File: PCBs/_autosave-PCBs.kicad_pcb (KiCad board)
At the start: 4 copper layers, 44.5 x 15.5 mm, 8 parts, among them P1 Input 1x2, P2 Output 1x2, U1 TPS62172DSGR

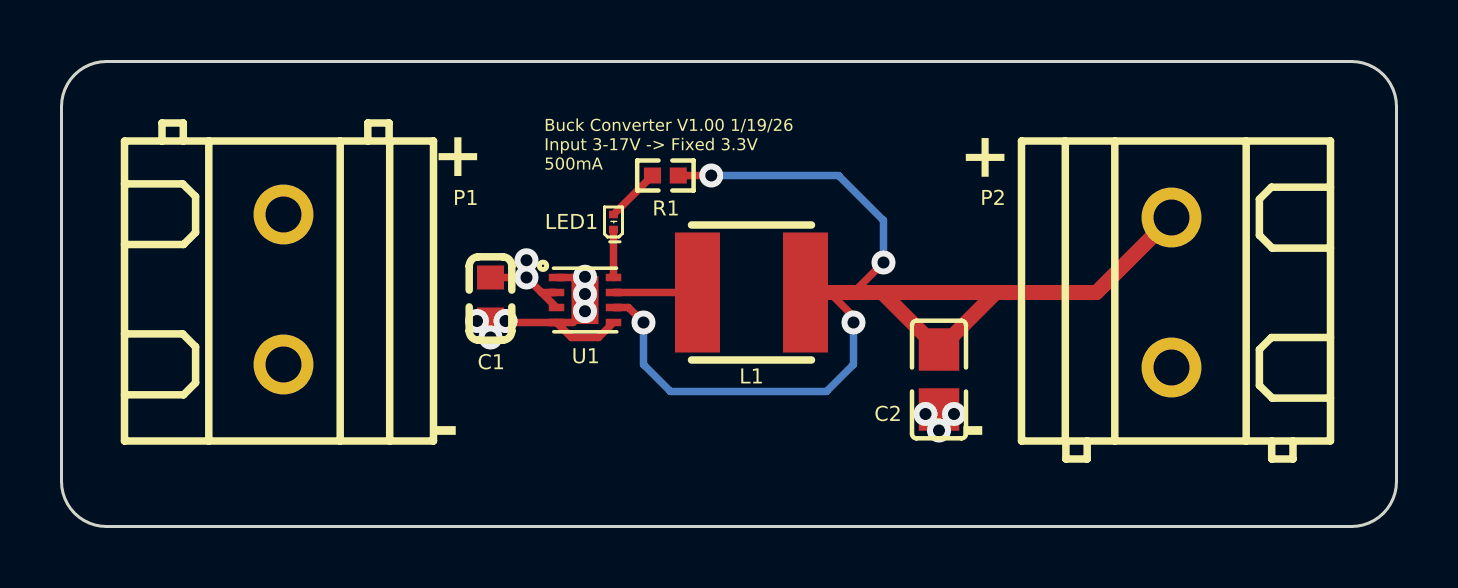
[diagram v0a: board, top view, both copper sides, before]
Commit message: buck converter done
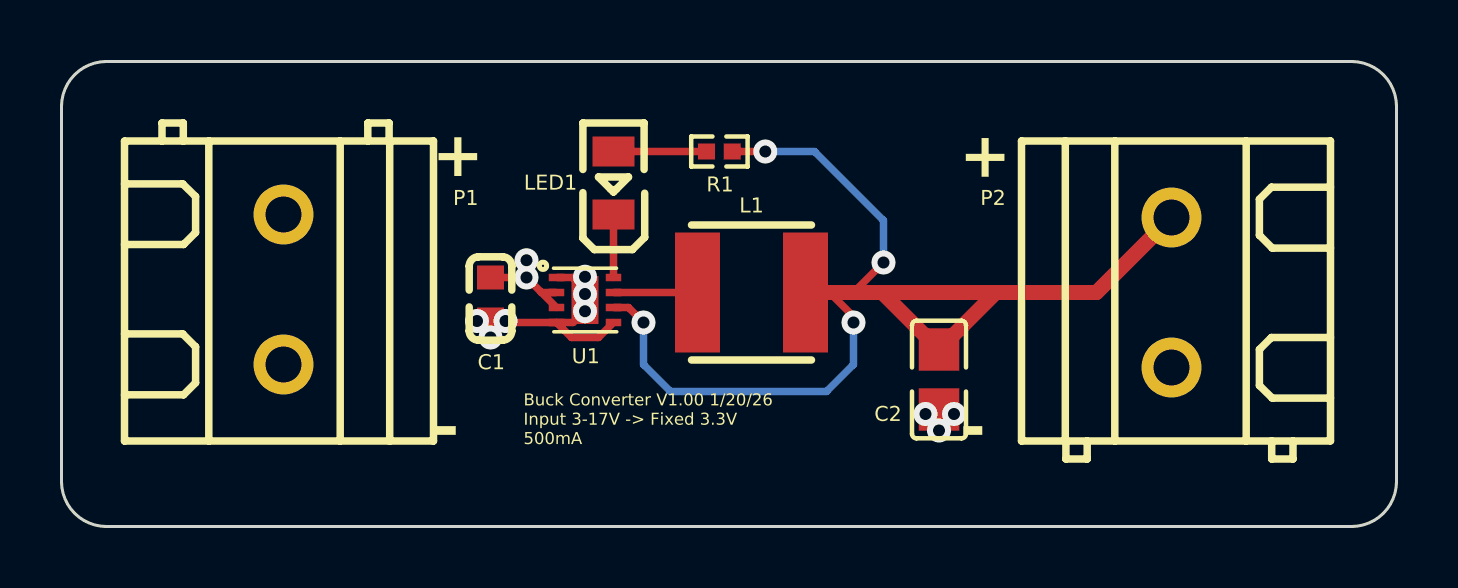
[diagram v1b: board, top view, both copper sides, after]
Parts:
- LED1: footprint EasyEDA2KicadFootprints:LED-SMD_L0.7-W0.4-RD_GREEN -> EasyEDA2KicadFootprints:LED0805-R-RD
- moved R1 1.97 mm to (150.9, 110.0)
- moved LED1 1.30 mm to (147.4, 111.0)
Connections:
- LED1 pad 1: Net-(LED1-K) -> Net-(LED1-A)
- LED1 pad 2: Net-(LED1-A) -> Net-(LED1-K)
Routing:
- net VCCOUT: track 43.2 -> 41.8 mm
- net Net-(LED1-A): track 1.84 -> 3.10 mm
- net Net-(LED1-K): track 1.60 -> 2.10 mm
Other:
- board text added: "Buck Converter V1.00 1/20/26 Input 3-17V -> Fixed 3.3V 500mA"
- board text removed: "Buck Converter V1.00 1/19/26 Input 3-17V -> Fixed 3.3V 500mA"
